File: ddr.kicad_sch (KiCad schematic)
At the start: 27 parts, among them U801 MT41K256M16TW

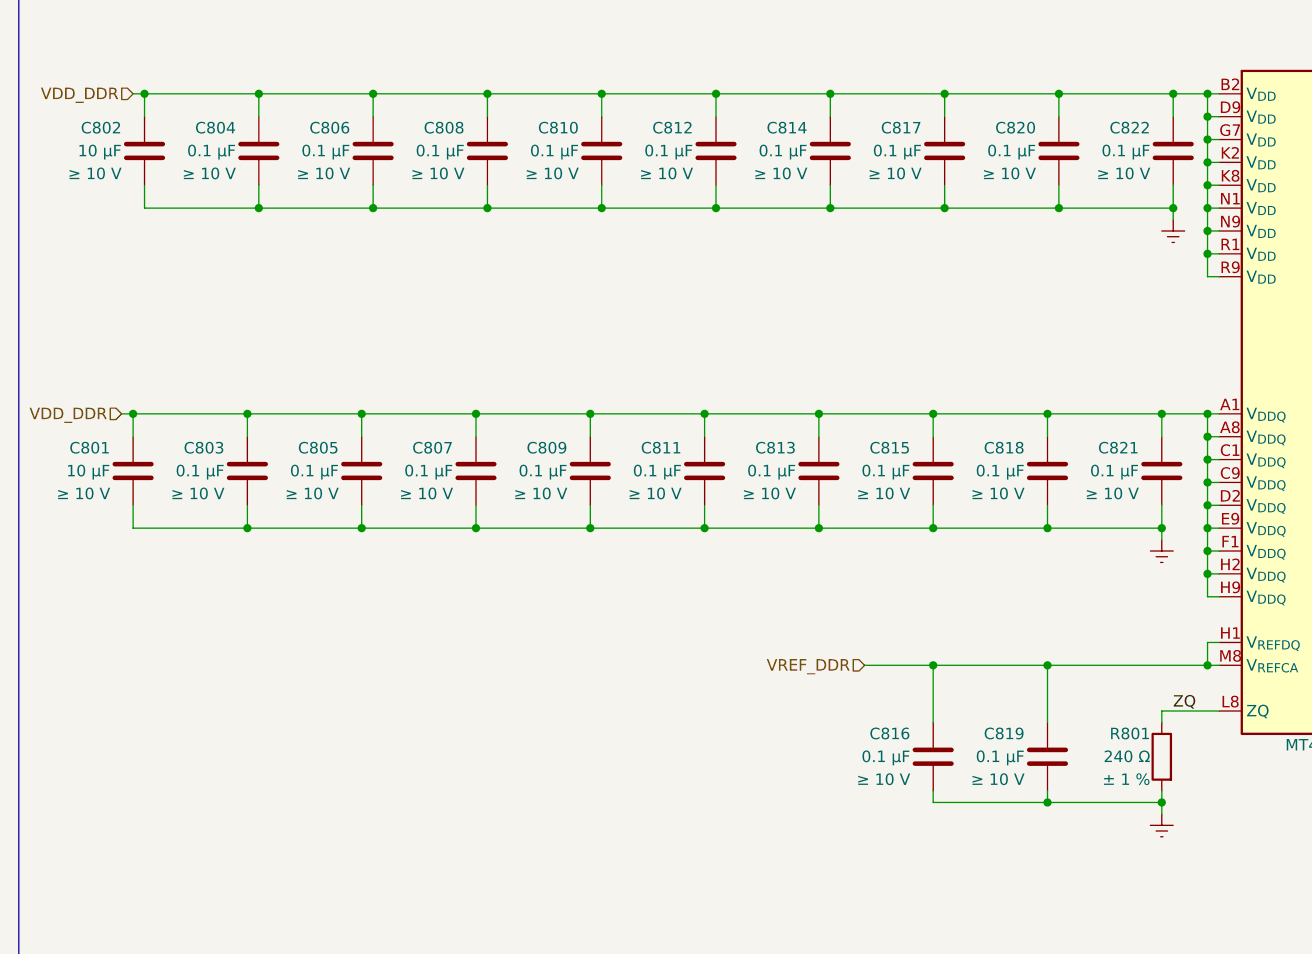
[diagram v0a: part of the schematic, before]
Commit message: Fix component values
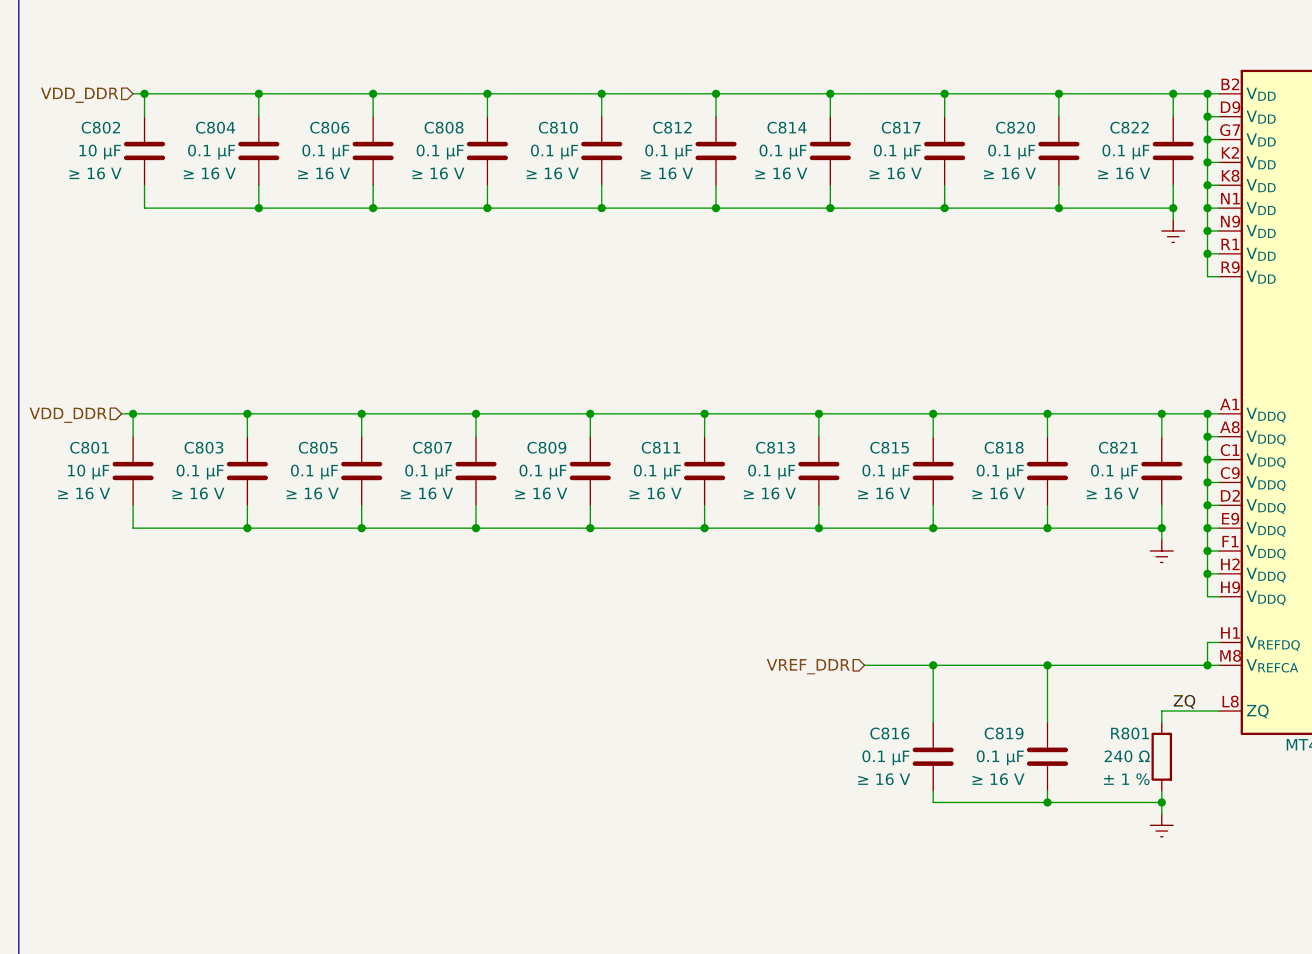
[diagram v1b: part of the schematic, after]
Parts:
- C801, C802, C803, C804, C805, C806, C807, C808, C809, C810, C811, C812, C813, C814, C815, C816, C817, C818, C819, C820, C821, C822: Voltage rating ≥ 10 V -> ≥ 16 V

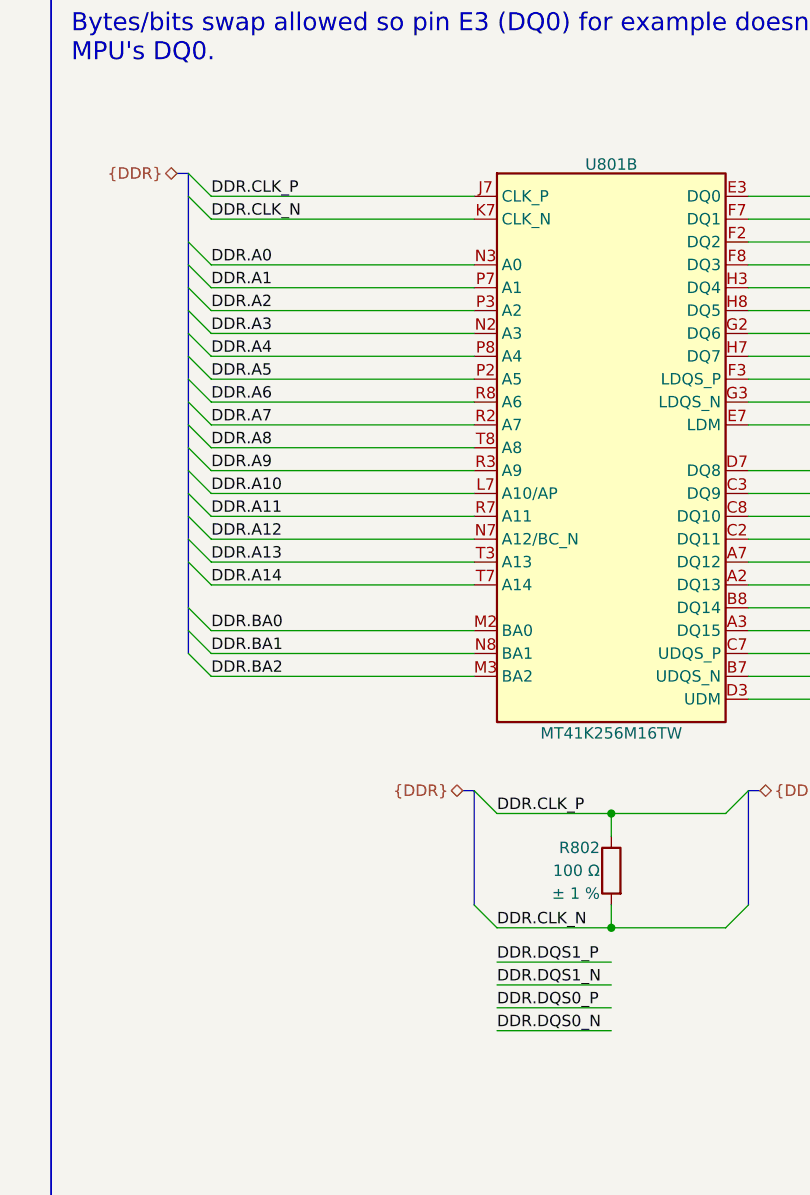
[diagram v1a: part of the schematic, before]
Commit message: Refactor schematics
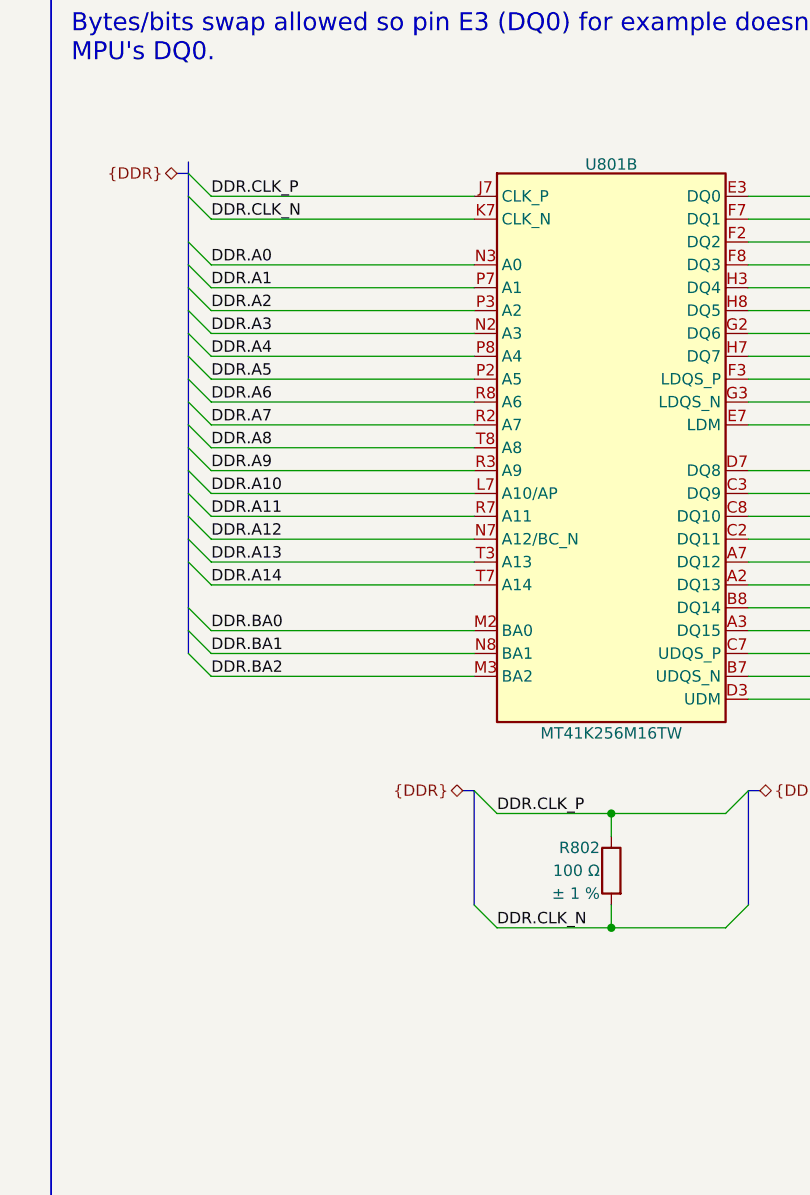
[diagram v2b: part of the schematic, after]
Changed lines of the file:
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@@
 		)
 	)
+	(bus
+		(pts
+			(xy 200.66 87.63) (xy 200.66 88.9)
+		)
+		(stroke
+			(width 0)
+			(type default)
+		)
+	)
 	(wire
 		(pts
@@
 	(wire
 		(pts
-			(xy 234.95 176.53) (xy 247.65 176.53)
-		)
-		(stroke
-			(width 0)
-			(type default)
-		)
-	)
-	(wire
-		(pts
 			(xy 176.53 100.33) (xy 177.8 100.33)
 		)
@@
 		)
 	)
-	(wire
-		(pts
-			(xy 234.95 184.15) (xy 247.65 184.15)
-		)
-		(stroke
-			(width 0)
-			(type default)
-		)
-	)
 	(bus
 		(pts
@@
 	(wire
 		(pts
-			(xy 234.95 179.07) (xy 247.65 179.07)
-		)
-		(stroke
-			(width 0)
-			(type default)
-		)
-	)
-	(wire
-		(pts
 			(xy 331.47 134.62) (xy 365.76 134.62)
 		)
@@
 	(wire
 		(pts
-			(xy 234.95 181.61) (xy 247.65 181.61)
-		)
-		(stroke
-			(width 0)
-			(type default)
-		)
-	)
-	(wire
-		(pts
 			(xy 177.8 102.87) (xy 177.8 105.41)
 		)
@@
 		)
 	)
-	(label "DDR.DQS0_P"
-		(at 234.95 181.61 0)
-		(effects
-			(font
-				(size 1.27 1.27)
-			)
-			(justify left bottom)
-		)
-	)
 	(label "DDR.A5"
 		(at 203.2 111.76 0)
@@
 		)
 	)
-	(label "DDR.DQS1_P"
-		(at 234.95 176.53 0)
-		(effects
-			(font
-				(size 1.27 1.27)
-			)
-			(justify left bottom)
-		)
-	)
 	(label "DDR.A8"
 		(at 203.2 119.38 0)
@@
 		)
 	)
-	(label "DDR.DQS1_N"
-		(at 234.95 179.07 0)
-		(effects
-			(font
-				(size 1.27 1.27)
-			)
-			(justify left bottom)
-		)
-	)
 	(label "DDR.A9"
 		(at 203.2 121.92 0)
@@
 		)
 	)
-	(label "DDR.DQS0_N"
-		(at 234.95 184.15 0)
-		(effects
-			(font
-				(size 1.27 1.27)
-			)
-			(justify left bottom)
-		)
-	)
 	(label "DDR.DQ10"
 		(at 297.18 106.68 180)
@@
 		)
 	)
-	(rule_area
-		(polyline
-			(pts
-				(xy 252.73 158.75) (xy 255.27 158.75) (xy 255.27 173.99) (xy 252.73 173.99)
-			)
-			(stroke
-				(width 0)
-				(type dash)
-			)
-			(fill
-				(type none)
-			)
-		)
-	)
 	(netclass_flag ""
 		(length 2.54)
 		(shape round)
-		(at 254 158.75 0)
+		(at 200.66 87.63 0)
 		(fields_autoplaced yes)
 		(effects
@@
 			(justify left bottom)
 		)
-		(property "Netclass" "DDR_PAIR"
-			(at 254.6985 156.21 0)
-			(effects
-				(font
-					(size 1.27 1.27)
-				)
-				(justify left)
-			)
-		)
-		(property "Component Class" ""
-			(at -49.53 3.81 0)
-			(effects
-				(font
-					(size 1.27 1.27)
-					(italic yes)
-				)
-			)
-		)
-	)
-	(netclass_flag ""
-		(length 2.54)
-		(shape round)
-		(at 247.65 176.53 270)
-		(effects
-			(font
-				(size 1.27 1.27)
-			)
-			(justify right bottom)
-		)
-		(property "Netclass" "DDR_PAIR"
-			(at 250.952 176.53 0)
-			(effects
-				(font
-					(size 1.27 1.27)
-				)
-				(justify left)
-			)
-		)
-		(property "Component Class" ""
-			(at -55.88 21.59 0)
-			(effects
-				(font
-					(size 1.27 1.27)
-					(italic yes)
-				)
-			)
-		)
-	)
-	(netclass_flag ""
-		(length 2.54)
-		(shape round)
-		(at 247.65 184.15 270)
-		(effects
-			(font
-				(size 1.27 1.27)
-			)
-			(justify right bottom)
-		)
-		(property "Netclass" "DDR_PAIR"
-			(at 250.952 184.15 0)
-			(effects
-				(font
-					(size 1.27 1.27)
-				)
-				(justify left)
-			)
-		)
-		(property "Component Class" ""
-			(at -55.88 29.21 0)
-			(effects
-				(font
-					(size 1.27 1.27)
-					(italic yes)
-				)
-			)
-		)
-	)
-	(netclass_flag ""
-		(length 2.54)
-		(shape round)
-		(at 247.65 179.07 270)
-		(effects
-			(font
-				(size 1.27 1.27)
-			)
-			(justify right bottom)
-		)
-		(property "Netclass" "DDR_PAIR"
-			(at 250.952 179.07 0)
-			(effects
-				(font
-					(size 1.27 1.27)
-				)
-				(justify left)
-			)
-		)
-		(property "Component Class" ""
-			(at -55.88 24.13 0)
-			(effects
-				(font
-					(size 1.27 1.27)
-					(italic yes)
-				)
-			)
-		)
-	)
-	(netclass_flag ""
-		(length 2.54)
-		(shape round)
-		(at 247.65 181.61 270)
-		(effects
-			(font
-				(size 1.27 1.27)
-			)
-			(justify right bottom)
-		)
-		(property "Netclass" "DDR_PAIR"
-			(at 250.952 181.61 0)
+		(property "Netclass" "DDR"
+			(at 201.3585 85.09 0)
 			(effects
 				(font
@@
 		)
 		(property "Component Class" ""
-			(at -55.88 26.67 0)
+			(at -102.87 -67.31 0)
 			(effects
 				(font

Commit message: Clean-up schematics
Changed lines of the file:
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@@
 		)
 	)
-	(text_box "Pinout according to STM32MP135F-DK.\n\nBytes/bits swap allowed so pin E3 (DQ0) for example doesn't have to connect to MPU's DQ0."
+	(text_box "Pinout according to STM32MP135F-DK.\nOn-Die-Termination on DQ/DQS/DM lines.\nBytes/bits swap allowed so pin E3 (DQ0) for example doesn't have to connect to MPU's DQ0."
 		(exclude_from_sim no)
 		(at 186.69 63.5 0)
